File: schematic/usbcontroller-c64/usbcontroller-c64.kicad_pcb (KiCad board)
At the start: 2 copper layers, 25 x 61 mm, 17 parts, among them J1 Conn_01x20_Socket, J2 Conn_01x20_Socket, J3 Conn_01x06_Socket, J4 Conn_01x02_Socket, J5 Conn_01x02_Socket, Q1 PN2222A, Q2 PN2222A, Q3 PN2222A, Q4 PN2222A, Q5 PN2222A

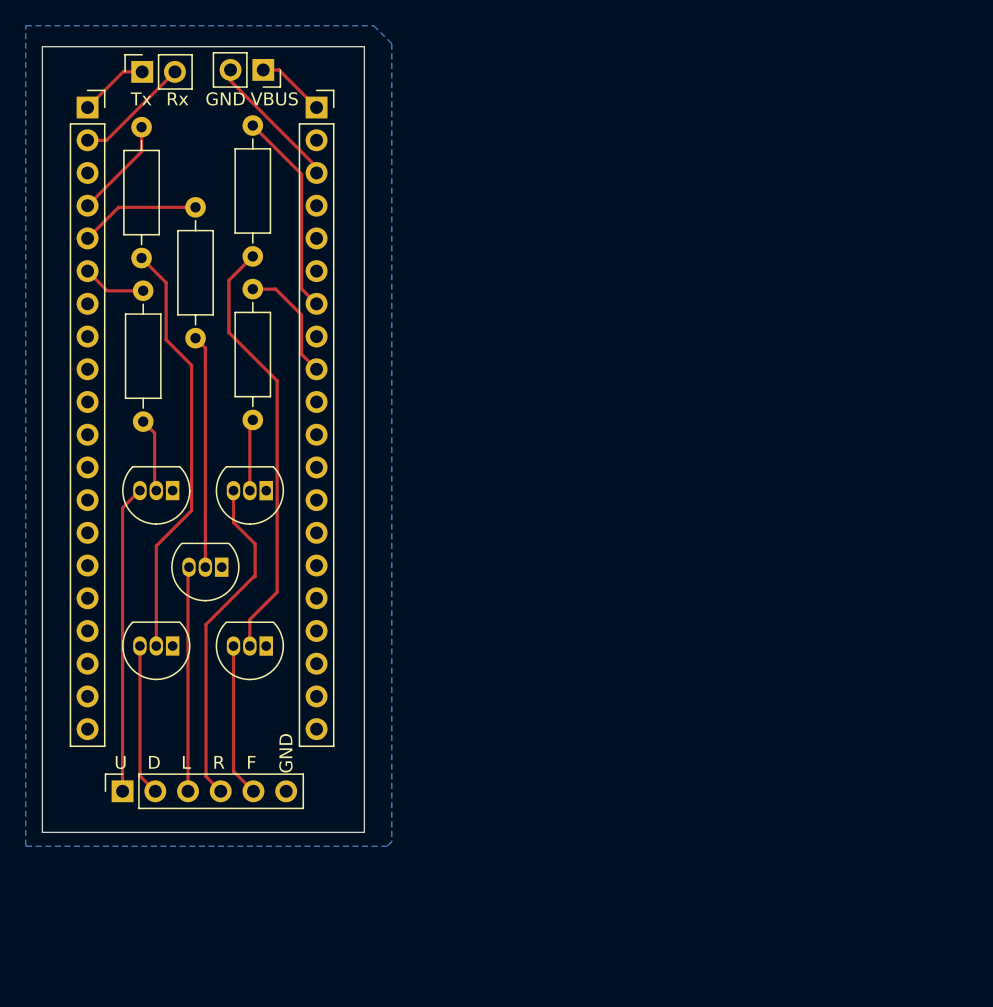
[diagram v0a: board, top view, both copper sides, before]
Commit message: update schematic to usb db9 connector and power
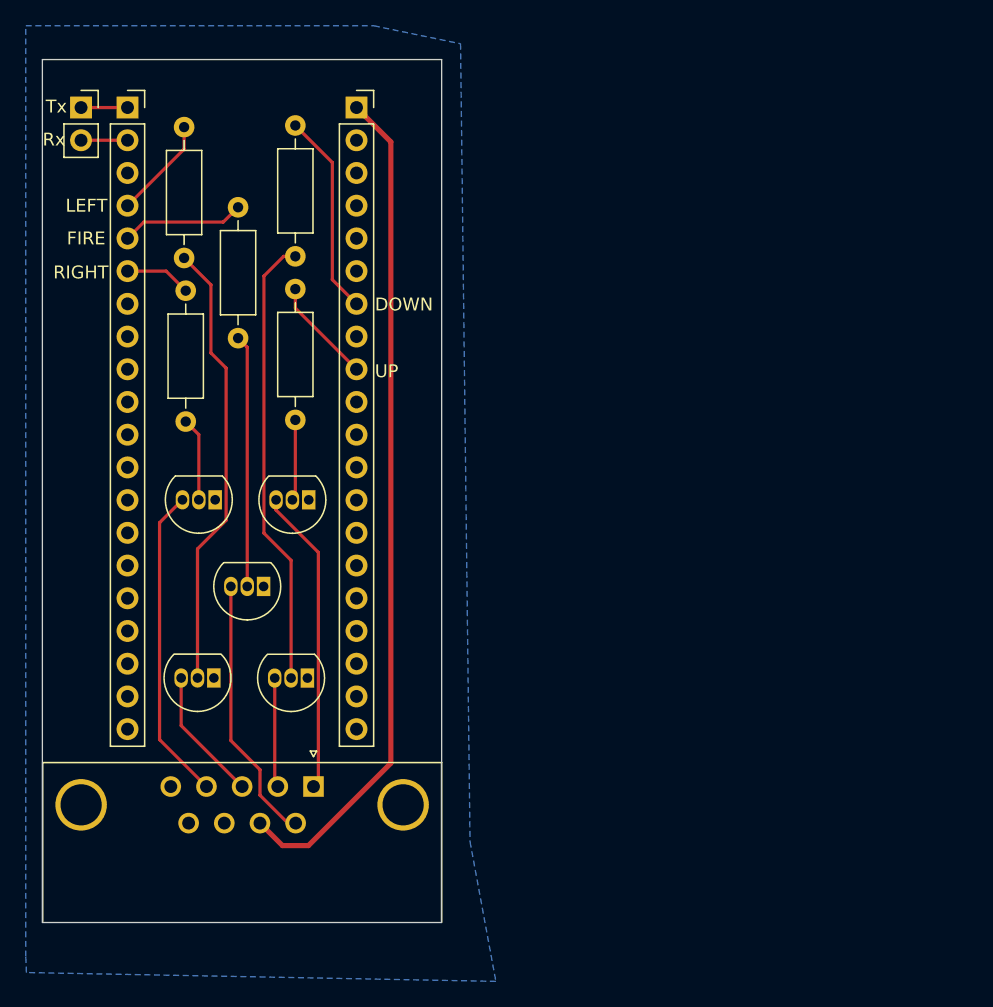
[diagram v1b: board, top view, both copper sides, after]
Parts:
- removed J3: Conn_01x06_Socket, Connector_PinSocket_2.54mm:PinSocket_1x06_P2.54mm_Vertical
- removed J4: Conn_01x02_Socket, Connector_PinSocket_2.54mm:PinSocket_1x02_P2.54mm_Vertical
- added J6: DE9_Receptacle, Connector_Dsub:DSUB-9_Female_Horizontal_P2.77x2.84mm_EdgePinOffset7.70mm_Housed_MountingHolesOffset9.12mm, F.Cu at (161.0, 146.4)
- moved G*** 11.3 mm to (155.4, 146.2)
- moved J5 5.50 mm to (143.0, 93.7), turned to 0 degrees
- moved Q1 4.05 mm to (153.3, 138.0)
- moved Q4 4.05 mm to (160.6, 138.0)
- moved Q2 3.58 mm to (157.2, 130.9)
- moved G*** 3.45 mm to (155.8, 99.6)
- moved Q5 3.38 mm to (160.7, 124.2)
- moved Q3 3.38 mm to (153.4, 124.2)
- moved R4 3.30 mm to (159.6, 95.1)
- moved R5 3.30 mm to (159.6, 107.8)
- moved R1 3.30 mm to (151.0, 95.2)
- moved R2 3.30 mm to (155.2, 101.5)
- moved R3 3.30 mm to (151.1, 107.9)
- moved J1 3.10 mm to (146.6, 93.7)
- moved J2 3.10 mm to (164.4, 93.7)
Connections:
- net Net-(J1-Pin_1) renamed /TX
- net Net-(J1-Pin_2) renamed /RX
- J2 pad 1: Net-(J2-Pin_1) -> /VBUS
- J2 pad 3: Net-(J2-Pin_3) -> GND
- Q1 pad 3: Net-(J3-Pin_2) -> /LEFT
- Q2 pad 3: Net-(J3-Pin_3) -> /FIRE
- Q3 pad 3: Net-(J3-Pin_1) -> /RIGHT
- Q4 pad 3: Net-(J3-Pin_5) -> /DOWN
- Q5 pad 3: Net-(J3-Pin_4) -> /UP
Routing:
- net /VBUS: track 0.00 -> 65.5 mm
- net Net-(J3-Pin_4): track 26.9 -> 0.00 mm
- net /RIGHT: track 0.00 -> 24.5 mm
- net Net-(J3-Pin_1): track 23.9 -> 0.00 mm
- net /UP: track 0.00 -> 23.8 mm
- net /FIRE: track 0.00 -> 21.5 mm
- net Net-(J3-Pin_3): track 17.7 -> 0.00 mm
- net Net-(J3-Pin_5): track 11.9 -> 0.00 mm
- net Net-(J3-Pin_2): track 11.8 -> 0.00 mm
- net Net-(J2-Pin_3): track 10.8 -> 0.00 mm
- net /LEFT: track 0.00 -> 10.4 mm
- net /DOWN: track 0.00 -> 8.52 mm
- net /RX: track 8.98 -> 3.61 mm
- net Net-(J2-Pin_1): track 5.35 -> 0.00 mm
- net Net-(Q1-B): track 32.9 -> 34.9 mm
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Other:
- board size 25 x 61 mm -> 31 x 67 mm
- board text added: "DOWN"
- board text added: "FIRE"
- board text added: "LEFT"
- board text added: "RIGHT"
- board text added: "UP"
- board text added: "v02"
- board text removed: "D"
- board text removed: "F"
- board text removed: "GND"
- board text removed: "L"
- board text removed: "R"
- board text removed: "U"
- board text removed: "VBUS"
- board text removed: "v01"

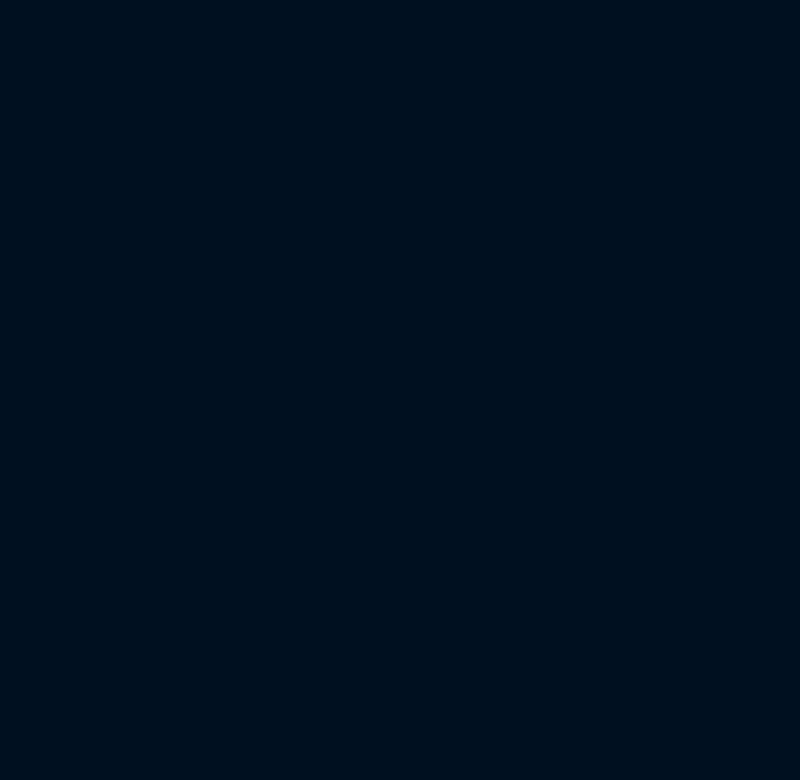
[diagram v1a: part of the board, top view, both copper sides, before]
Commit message: remove forked pico-sdk depeancy and get back on the normal one
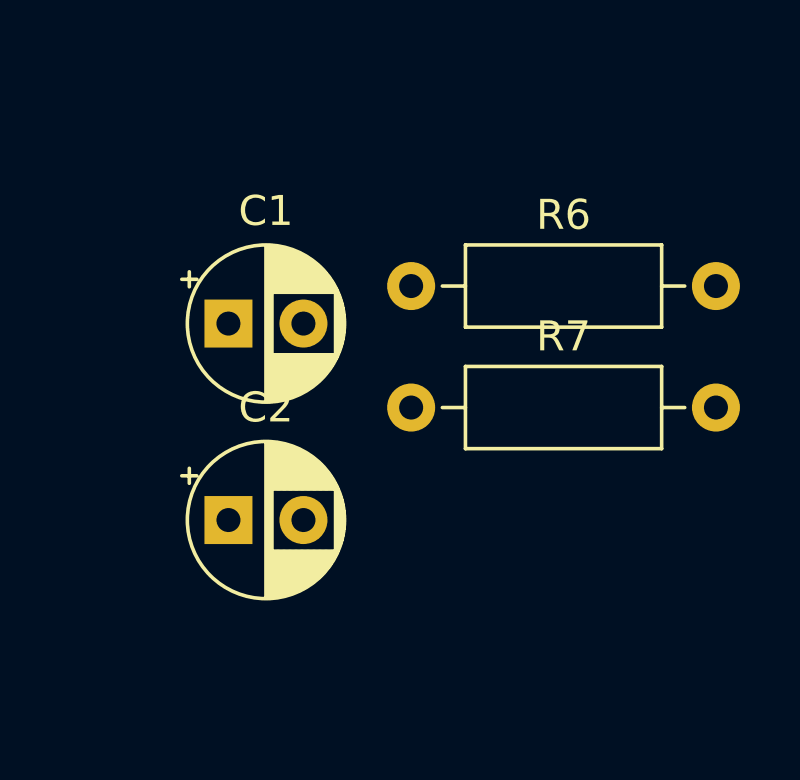
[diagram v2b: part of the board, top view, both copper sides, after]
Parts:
- added C1: 39pF, Capacitor_THT:CP_Radial_D5.0mm_P2.50mm, F.Cu at (194.7, 114.7)
- added C2: 39pF, Capacitor_THT:CP_Radial_D5.0mm_P2.50mm, F.Cu at (194.7, 121.2)
- added R6: 1K, Resistor_THT:R_Axial_DIN0207_L6.3mm_D2.5mm_P10.16mm_Horizontal, F.Cu at (200.8, 113.5)
- added R7: 1K, Resistor_THT:R_Axial_DIN0207_L6.3mm_D2.5mm_P10.16mm_Horizontal, F.Cu at (200.8, 117.5)
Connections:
- J6 pad 7: /VBUS -> Net-(D1-A)
